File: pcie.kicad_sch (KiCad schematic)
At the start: 27 parts, among them U15 XC7K160T-FFG676

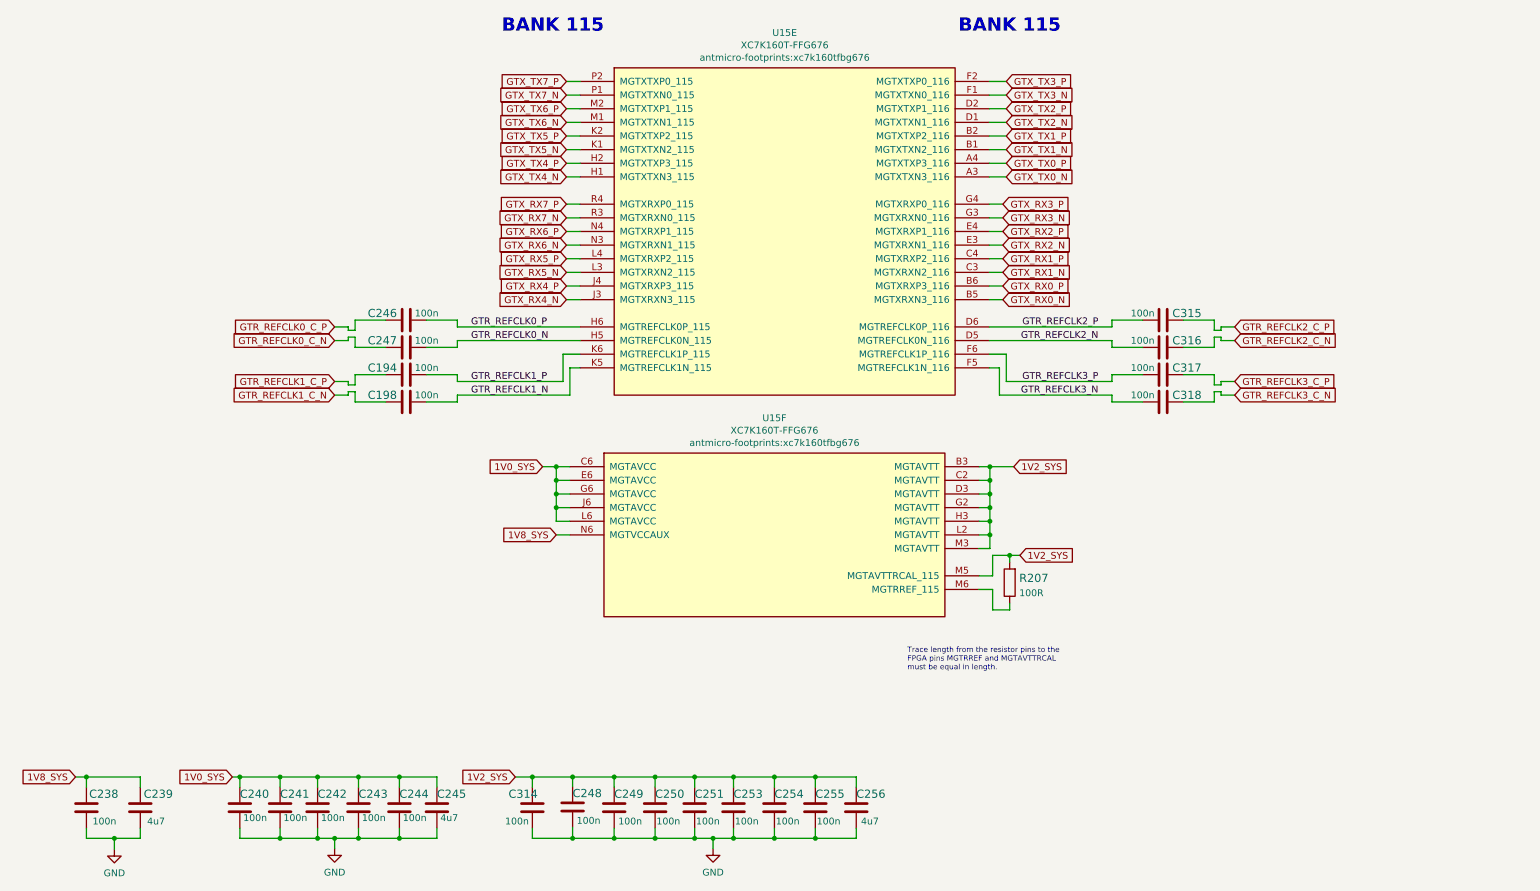
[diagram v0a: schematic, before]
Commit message: Rebase to Rev. 1.2.2
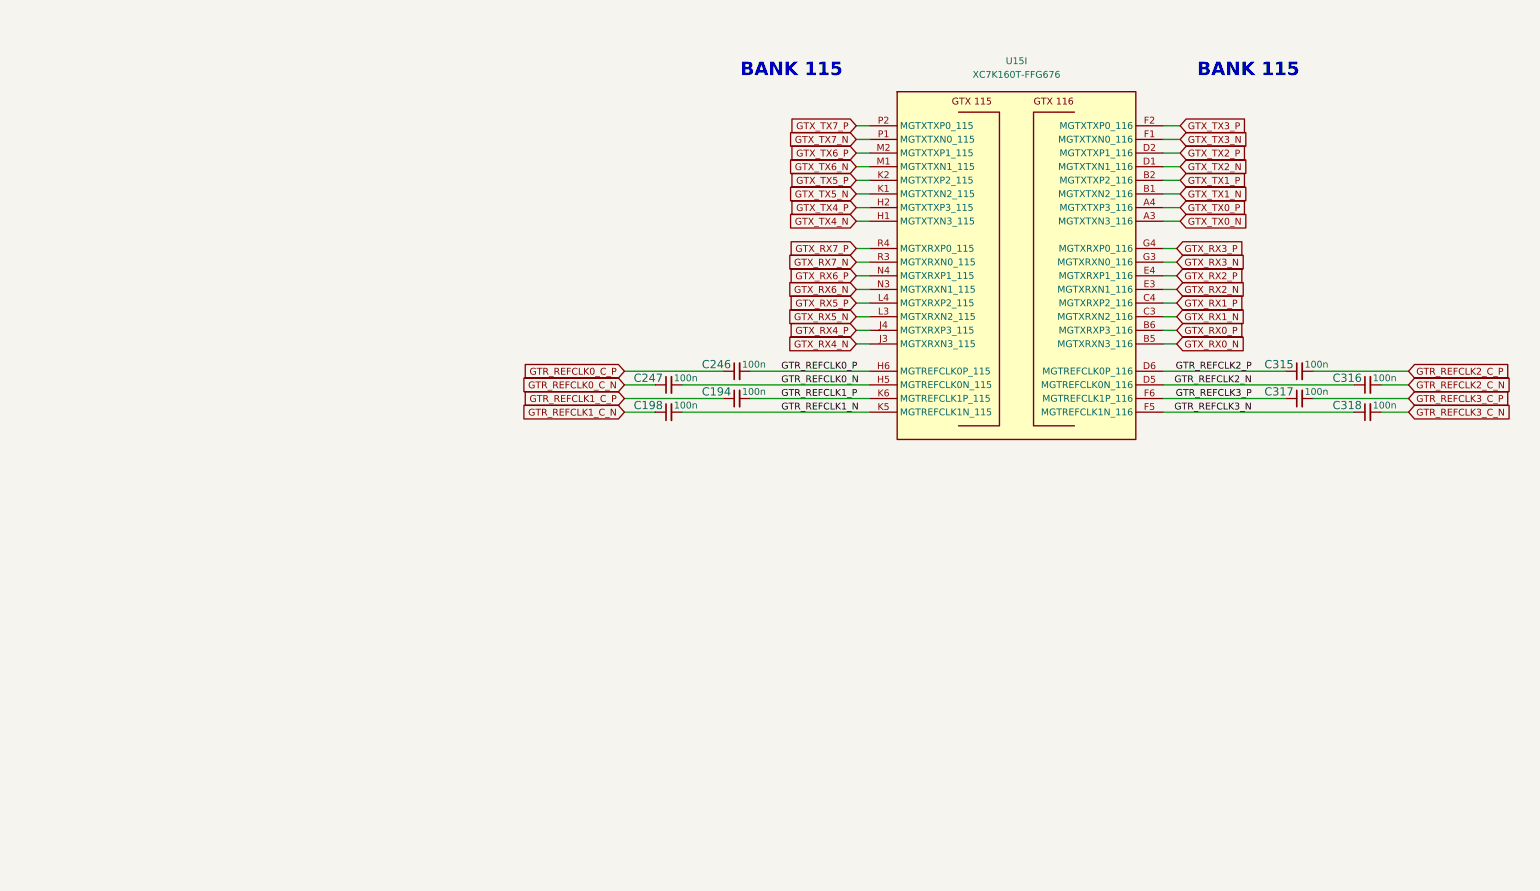
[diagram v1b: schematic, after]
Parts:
- removed C194, C198, C246, C247, C314, C315, C316, C317, C318: C_100n_0402, antmicro-footprints:0402-cap, symbol antmicroCapacitors0402:C_100n_0402
- removed C238, C240, C241, C242, C243, C244, C248, C249, C250, C251, C253, C254, C255: C_100n_0201, antmicro-footprints:0201-res, symbol antmicroCapacitorsmisc:C_100n_0201
- removed C239, C245, C256: C_4u7_0402, antmicro-footprints:0402-cap, symbol antmicroCapacitors0402:C_4u7_0402
- removed R207: R_100R_0402, antmicro-footprints:0402-res, symbol antmicroResistors0402:R_100R_0402
- removed U15: XC7K160T-FFG676, antmicro-footprints:xc7k160tfbg676, symbol data-center-dram-tester:XC7K160T-FFG676
- added C194, C198, C246, C247, C315, C316, C317, C318: C_100n_0402, data-center-rdimm-ddr4-tester-footprints:C_0402_1005Metric, symbol data-center-rdimm-ddr4-tester:C_100n_0402
- added U15: XC7K160T-FFG676, data-center-rdimm-ddr4-tester-footprints:BGA-676_27x27mm_Layout26x26_P1X1mm, symbol data-center-rdimm-ddr4-tester:XC7K160T-FFG676
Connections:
- net GTR_REFCLK0_C_N: now also C247.1
- net GTR_REFCLK0_C_P: now also C246.1
- net GTR_REFCLK0_N: now also C247.2, U15.H5 (MGTREFCLK0N_115)
- net GTR_REFCLK0_P: now also C246.2, U15.H6 (MGTREFCLK0P_115)
- net GTR_REFCLK1_C_N: now also C198.1
- net GTR_REFCLK1_C_P: now also C194.1
- net GTR_REFCLK1_N: now also C198.2, U15.K5 (MGTREFCLK1N_115)
- net GTR_REFCLK1_P: now also C194.2, U15.K6 (MGTREFCLK1P_115)
- net GTR_REFCLK2_C_N: now also C316.2
- net GTR_REFCLK2_C_P: now also C315.2
- net GTR_REFCLK2_N: now also C316.1, U15.D5 (MGTREFCLK0N_116)
- net GTR_REFCLK2_P: now also C315.1, U15.D6 (MGTREFCLK0P_116)
- net GTR_REFCLK3_C_N: now also C318.2
- net GTR_REFCLK3_C_P: now also C317.2
- net GTR_REFCLK3_N: now also C318.1, U15.F5 (MGTREFCLK1N_116)
- net GTR_REFCLK3_P: now also C317.1, U15.F6 (MGTREFCLK1P_116)
- net GTX_RX0_N: now also U15.B5 (MGTXRXN3_116)
- net GTX_RX0_P: now also U15.B6 (MGTXRXP3_116)
- net GTX_RX1_N: now also U15.C3 (MGTXRXN2_116)
- net GTX_RX1_P: now also U15.C4 (MGTXRXP2_116)
- net GTX_RX2_N: now also U15.E3 (MGTXRXN1_116)
- net GTX_RX2_P: now also U15.E4 (MGTXRXP1_116)
- net GTX_RX3_N: now also U15.G3 (MGTXRXN0_116)
- net GTX_RX3_P: now also U15.G4 (MGTXRXP0_116)
- net GTX_RX4_N: now also U15.J3 (MGTXRXN3_115)
- net GTX_RX4_P: now also U15.J4 (MGTXRXP3_115)
- net GTX_RX5_N: now also U15.L3 (MGTXRXN2_115)
- net GTX_RX5_P: now also U15.L4 (MGTXRXP2_115)
- net GTX_RX6_N: now also U15.N3 (MGTXRXN1_115)
- net GTX_RX6_P: now also U15.N4 (MGTXRXP1_115)
- net GTX_RX7_N: now also U15.R3 (MGTXRXN0_115)
- net GTX_RX7_P: now also U15.R4 (MGTXRXP0_115)
- net GTX_TX0_N: now also U15.A3 (MGTXTXN3_116)
- net GTX_TX0_P: now also U15.A4 (MGTXTXP3_116)
- net GTX_TX1_N: now also U15.B1 (MGTXTXN2_116)
- net GTX_TX1_P: now also U15.B2 (MGTXTXP2_116)
- net GTX_TX2_N: now also U15.D1 (MGTXTXN1_116)
- net GTX_TX2_P: now also U15.D2 (MGTXTXP1_116)
- net GTX_TX3_N: now also U15.F1 (MGTXTXN0_116)
- net GTX_TX3_P: now also U15.F2 (MGTXTXP0_116)
- net GTX_TX4_N: now also U15.H1 (MGTXTXN3_115)
- net GTX_TX4_P: now also U15.H2 (MGTXTXP3_115)
- net GTX_TX5_N: now also U15.K1 (MGTXTXN2_115)
- net GTX_TX5_P: now also U15.K2 (MGTXTXP2_115)
- net GTX_TX6_N: now also U15.M1 (MGTXTXN1_115)
- net GTX_TX6_P: now also U15.M2 (MGTXTXP1_115)
- net GTX_TX7_N: now also U15.P1 (MGTXTXN0_115)
- net GTX_TX7_P: now also U15.P2 (MGTXTXP0_115)
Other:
- note removed: "Trace length from the resistor pins to the FPGA pins MGTRREF and MGTAVTTRCAL must be equal in length."

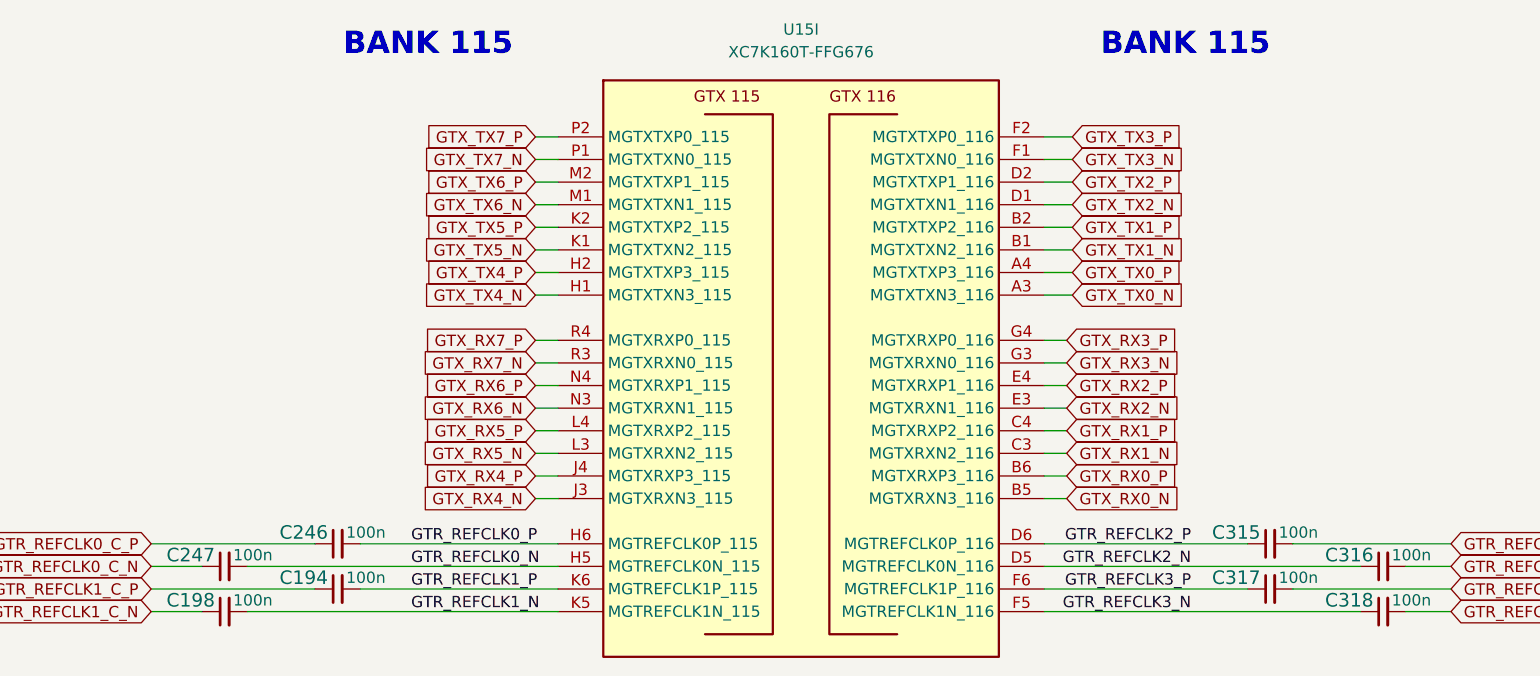
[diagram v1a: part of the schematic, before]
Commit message: Add PCIe x4 connector to the schematic
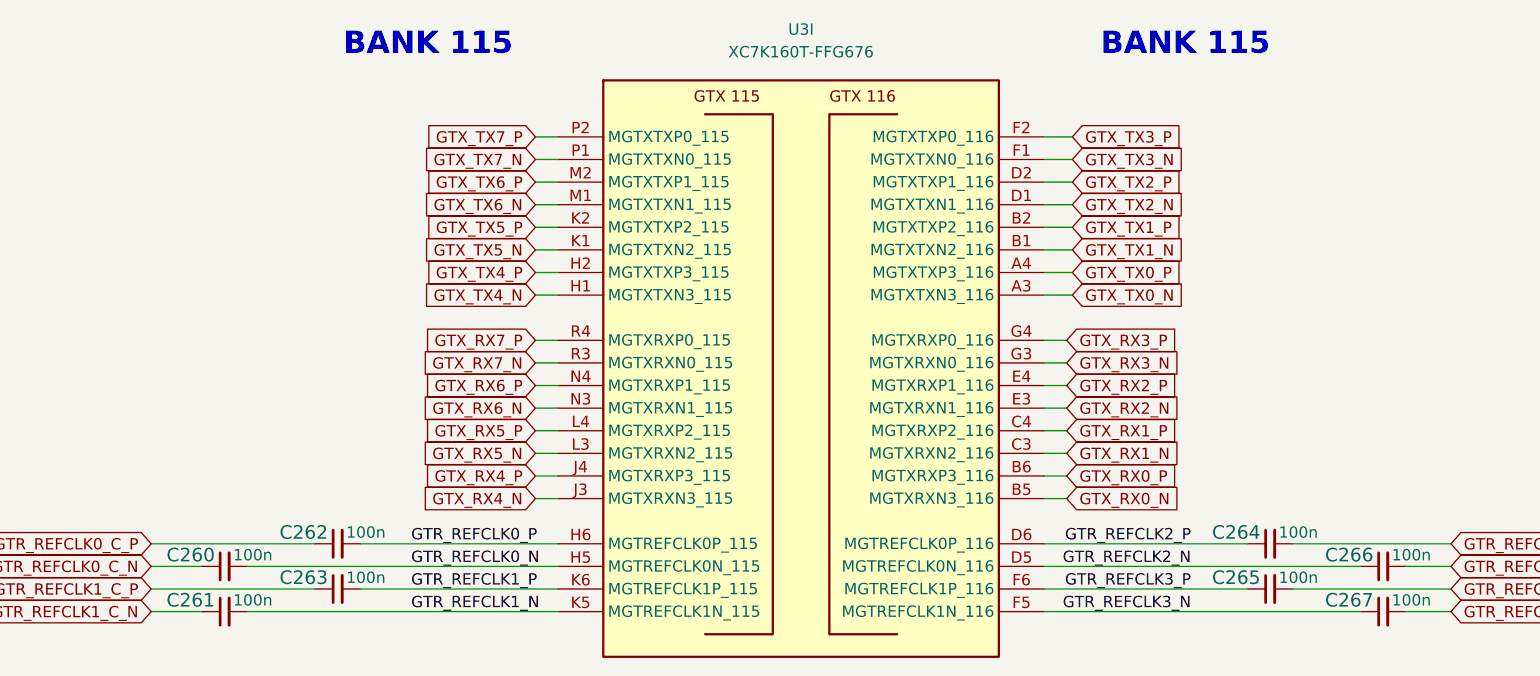
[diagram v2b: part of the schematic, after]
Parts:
- renumbered C247 to C260, C198 to C261, C246 to C262, C194 to C263, C315 to C264, C317 to C265, C316 to C266, C318 to C267, U15 to U3
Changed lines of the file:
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@@
   (symbol (lib_id "data-center-rdimm-ddr4-tester:C_100n_0402") (at 144.78 99.06 0) (unit 1)
     (in_bom yes) (on_board yes)
-    (property "Reference" "C246" (id 0) (at 143.51 97.79 0)
+    (property "Reference" "C262" (id 0) (at 143.51 97.79 0)
       (effects (font (size 1.524 1.524)))
     )
@@
   (symbol (lib_id "data-center-rdimm-ddr4-tester:C_100n_0402") (at 249.555 104.14 0) (mirror x) (unit 1)
     (in_bom yes) (on_board yes)
-    (property "Reference" "C317" (id 0) (at 248.285 102.87 0)
+    (property "Reference" "C265" (id 0) (at 248.285 102.87 0)
       (effects (font (size 1.524 1.524)))
     )
@@
   (symbol (lib_id "data-center-rdimm-ddr4-tester:C_100n_0402") (at 132.08 106.68 0) (unit 1)
     (in_bom yes) (on_board yes)
-    (property "Reference" "C198" (id 0) (at 130.81 105.41 0)
+    (property "Reference" "C261" (id 0) (at 130.81 105.41 0)
       (effects (font (size 1.524 1.524)))
     )
@@
   (symbol (lib_id "data-center-rdimm-ddr4-tester:C_100n_0402") (at 144.78 104.14 0) (unit 1)
     (in_bom yes) (on_board yes)
-    (property "Reference" "C194" (id 0) (at 143.51 102.87 0)
+    (property "Reference" "C263" (id 0) (at 143.51 102.87 0)
       (effects (font (size 1.524 1.524)))
     )
@@
   (symbol (lib_id "data-center-rdimm-ddr4-tester:C_100n_0402") (at 262.255 101.6 0) (mirror x) (unit 1)
     (in_bom yes) (on_board yes)
-    (property "Reference" "C316" (id 0) (at 260.985 100.33 0)
+    (property "Reference" "C266" (id 0) (at 260.985 100.33 0)
       (effects (font (size 1.524 1.524)))
     )
@@
   (symbol (lib_id "data-center-rdimm-ddr4-tester:XC7K160T-FFG676") (at 172.085 53.34 0) (unit 9)
     (in_bom yes) (on_board yes) (fields_autoplaced)
-    (property "Reference" "U15" (id 0) (at 199.39 41.275 0))
+    (property "Reference" "U3" (id 0) (at 199.39 41.275 0))
     (property "Value" "XC7K160T-FFG676" (id 1) (at 199.39 43.815 0)
       (effects (font (size 1.27 1.27) (thickness 0.15)))
@@
   (symbol (lib_id "data-center-rdimm-ddr4-tester:C_100n_0402") (at 262.255 106.68 0) (mirror x) (unit 1)
     (in_bom yes) (on_board yes)
-    (property "Reference" "C318" (id 0) (at 260.985 105.41 0)
+    (property "Reference" "C267" (id 0) (at 260.985 105.41 0)
       (effects (font (size 1.524 1.524)))
     )
@@
   (symbol (lib_id "data-center-rdimm-ddr4-tester:C_100n_0402") (at 132.08 101.6 0) (unit 1)
     (in_bom yes) (on_board yes)
-    (property "Reference" "C247" (id 0) (at 130.81 100.33 0)
+    (property "Reference" "C260" (id 0) (at 130.81 100.33 0)
       (effects (font (size 1.524 1.524)))
     )
@@
   (symbol (lib_id "data-center-rdimm-ddr4-tester:C_100n_0402") (at 249.555 99.06 0) (mirror x) (unit 1)
     (in_bom yes) (on_board yes)
-    (property "Reference" "C315" (id 0) (at 248.285 97.79 0)
+    (property "Reference" "C264" (id 0) (at 248.285 97.79 0)
       (effects (font (size 1.524 1.524)))
     )
